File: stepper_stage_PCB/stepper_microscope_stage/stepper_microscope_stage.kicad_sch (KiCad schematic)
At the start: 27 parts, among them J1 Conn_01x04_Socket, J2 Screw_Terminal_01x04, J3 Screw_Terminal_01x04, J4 Conn_01x04_Socket, J5 Conn_01x04_Socket, SW1 SW_SPDT

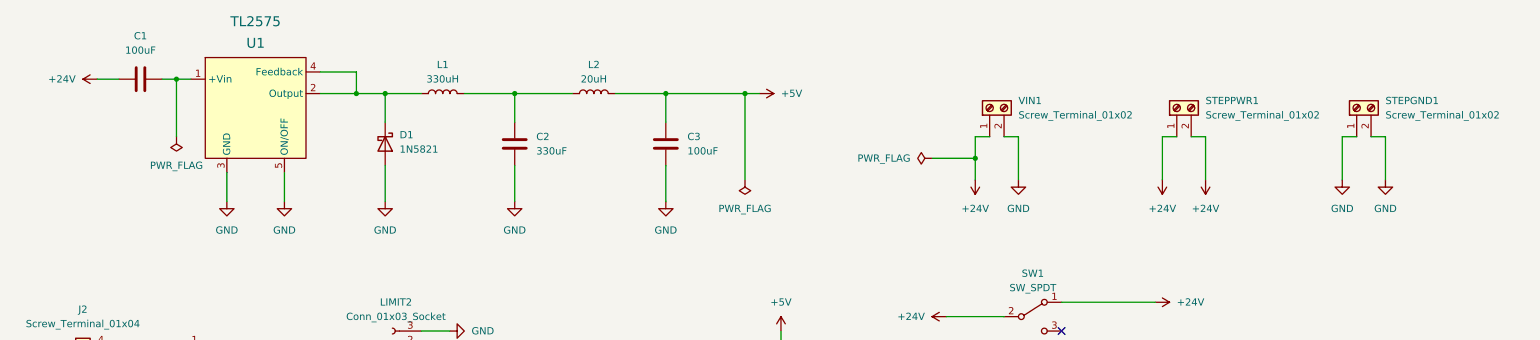
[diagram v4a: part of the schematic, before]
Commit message: Version 0
Updated PCB, milled that PCB, soldered parts to that PCB, updated code, works as expected except for the following functionalities listed below:
- Laser gates are non-operational as of yet. This leads to the following:
	- No homing functionality yet
	- No safety measures to ensure the steppers avoid grinding on their bearings
- True logarithmic speed control
- Suitable housing
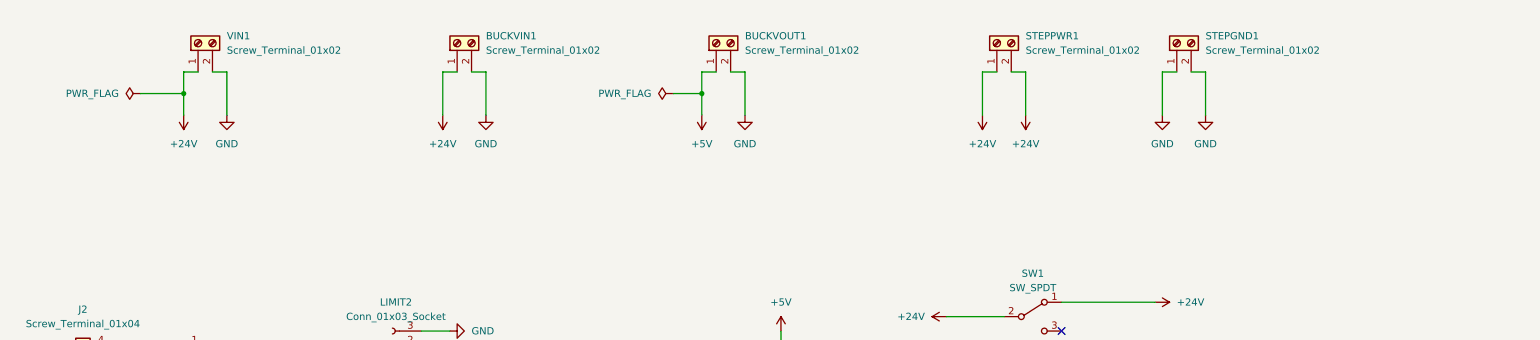
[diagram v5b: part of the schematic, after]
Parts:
- removed C1, C3: 100uF, Capacitor_SMD:CP_Elec_6.3x7.7, symbol Device:C
- removed C2: 330uF, Capacitor_SMD:CP_Elec_6.3x7.7, symbol Device:C
- removed D1: 1N5821, Diode_THT:D_DO-201AD_P12.70mm_Horizontal, symbol Device:D_Schottky
- removed L1: 330uH, Inductor_SMD:L_12x12mm_H6mm, symbol Device:L
- removed L2: 20uH, Inductor_SMD:L_Wuerth_HCI-1335, symbol Device:L
- removed TL2575: U1, Package_TO_SOT_SMD:TO-263-5_TabPin3, symbol TL2575:TL2575-xxIKTTR
- added BUCKVIN1, BUCKVOUT1: Screw_Terminal_01x02, TerminalBlock:TerminalBlock_Altech_AK300-2_P5.00mm, symbol Connector:Screw_Terminal_01x02
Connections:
- net +24V: now also BUCKVIN1.1 (Pin_1)
- net +5V: now also BUCKVOUT1.1 (Pin_1)
- net GND: now also BUCKVIN1.2 (Pin_2), BUCKVOUT1.2 (Pin_2)
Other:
- moved on the sheet: STEPGND1, STEPPWR1, VIN1
